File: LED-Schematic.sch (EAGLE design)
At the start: 12 parts, among them J1 POWER_JACKPTH, Q1 SUP75N06-08, Q2 SUP75N06-08, Q3 SUP75N06-08

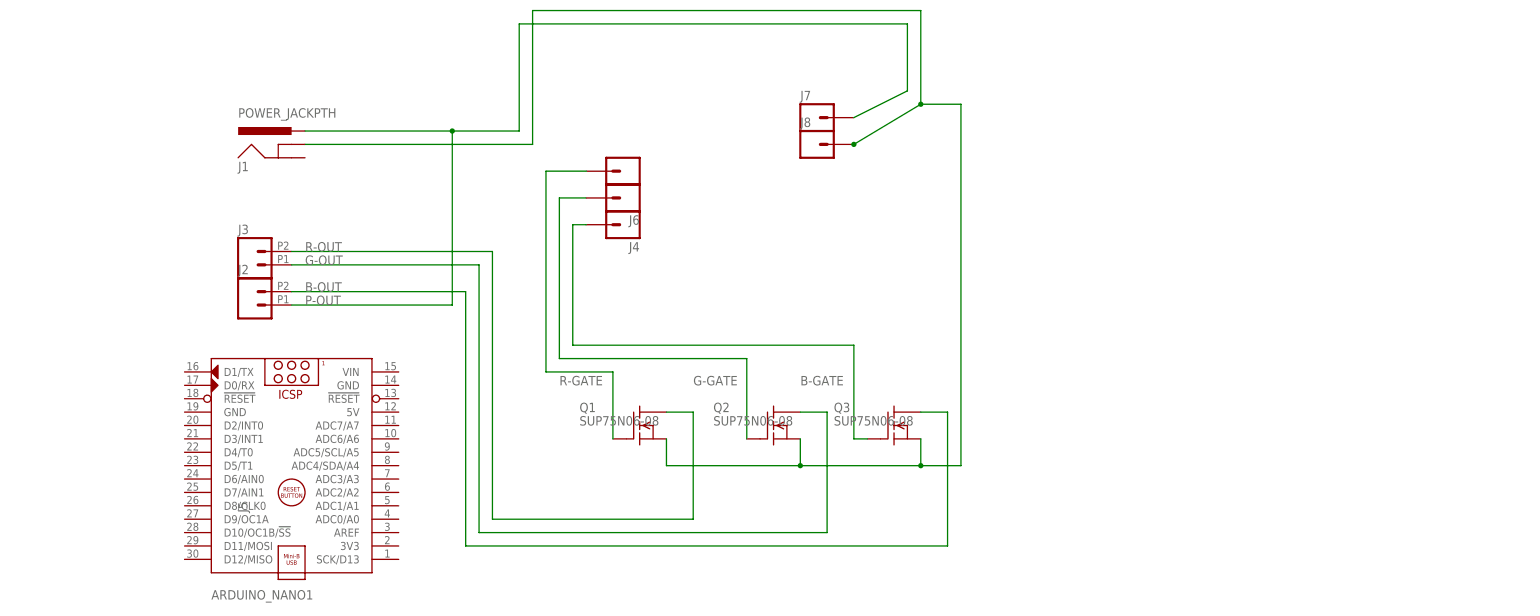
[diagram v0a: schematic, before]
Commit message: Added arduino to schematic, added PCB board, added gitignore
Signed-off-by: Maximilian Pult <it@optik-riede.de>
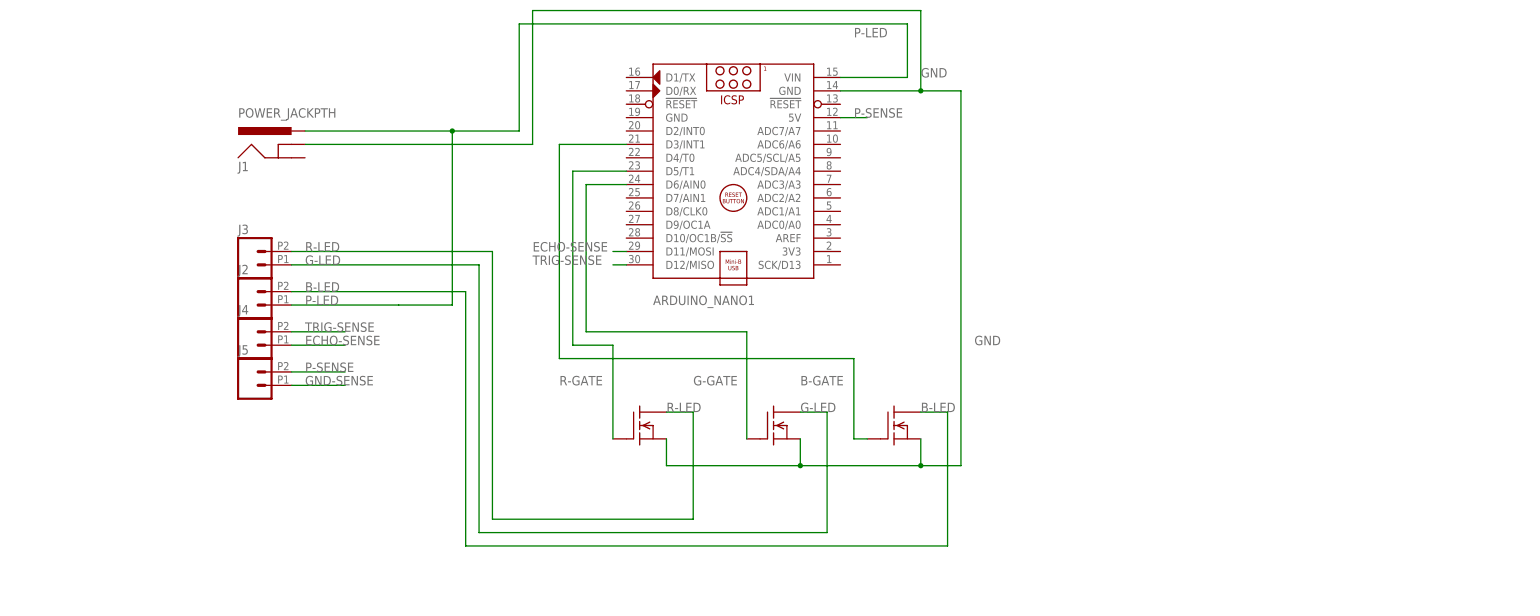
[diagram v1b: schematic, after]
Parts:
- removed J6, J7, J8: (no value), SparkFun-Connectors:M01SNAP-FEMALE
- J4, J5: device SparkFun-Connectors:M01SNAP-FEMALE -> SparkFun-Connectors:M022.54MM_SCREWTERM
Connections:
- net B-OUT renamed B-LED
- net G-OUT renamed G-LED
- net R-OUT renamed R-LED
- removed net N$3: J1.GNDBREAK, J8.1, Q1.S, Q2.S, Q3.S
- removed net P-OUT: J1.PWR, J2.1, J7.1
- new net ECHO-SENSE: ARDUINO_NANO1.D11/MOSI, J4.1
- new net GND: ARDUINO_NANO1.GND@2, J1.GNDBREAK, Q1.S, Q2.S, Q3.S
- new net GND-SENSE: J5.1
- new net P-LED: ARDUINO_NANO1.VIN, J1.PWR, J2.1
- new net P-SENSE: ARDUINO_NANO1.5V, J5.2
- new net TRIG-SENSE: ARDUINO_NANO1.D12/MISO, J4.2
- net B-GATE: now also ARDUINO_NANO1.D3/INT1; no longer J4.1
- net G-GATE: now also ARDUINO_NANO1.D6/AIN0; no longer J6.1
- net R-GATE: now also ARDUINO_NANO1.D5/T1; no longer J5.1
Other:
- moved on the sheet: ARDUINO_NANO1

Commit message: swapped mosfets to infineon IRLs
Signed-off-by: Maximilian Pult <it@optik-riede.de>
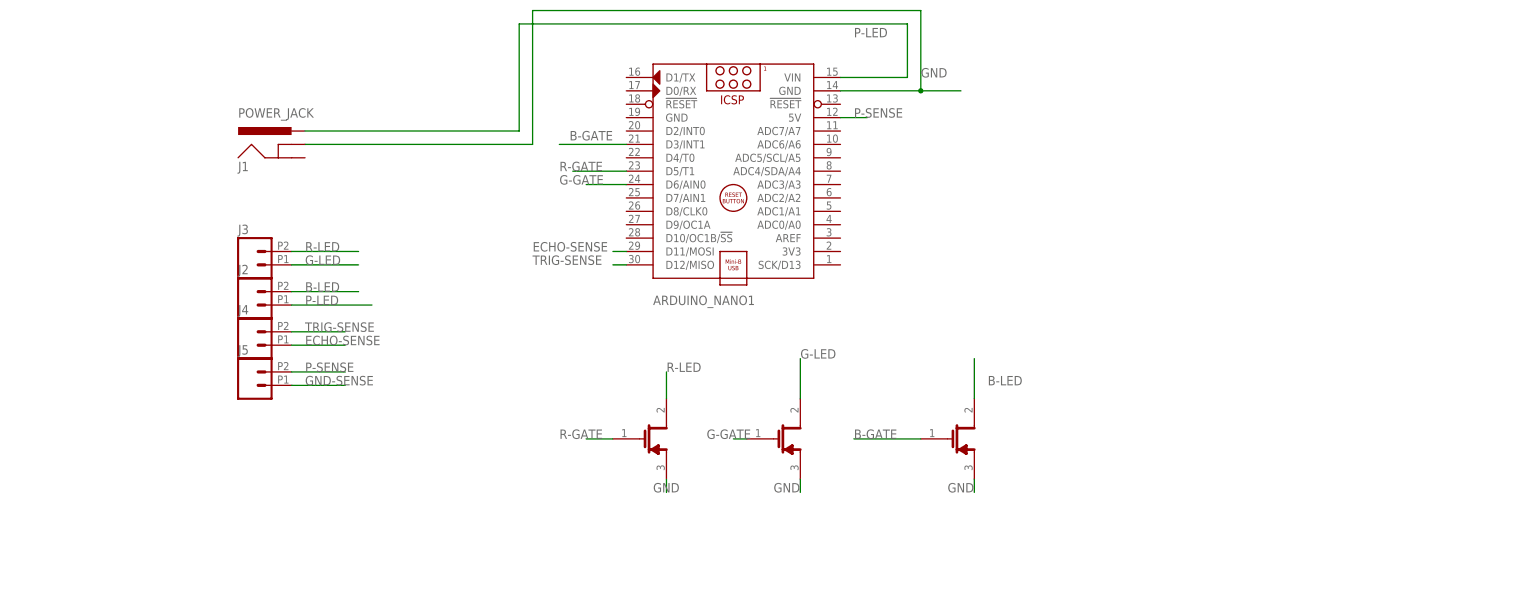
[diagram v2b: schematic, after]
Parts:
- J1: value POWER_JACKPTH -> POWER_JACK; device SparkFun-Connectors:POWER_JACKPTH -> SparkFun-Connectors:POWER_JACK
- Q1, Q2, Q3: value SUP75N06-08 -> INFINEON_IRLB8721PBFINFINEON_IRLB8721PBF_0_0; device transistor-fet:SUP75N06-08 -> Infineon - IRLB8721PbF:INFINEON_IRLB8721PBFINFINEON_IRLB8721PBF_0_0

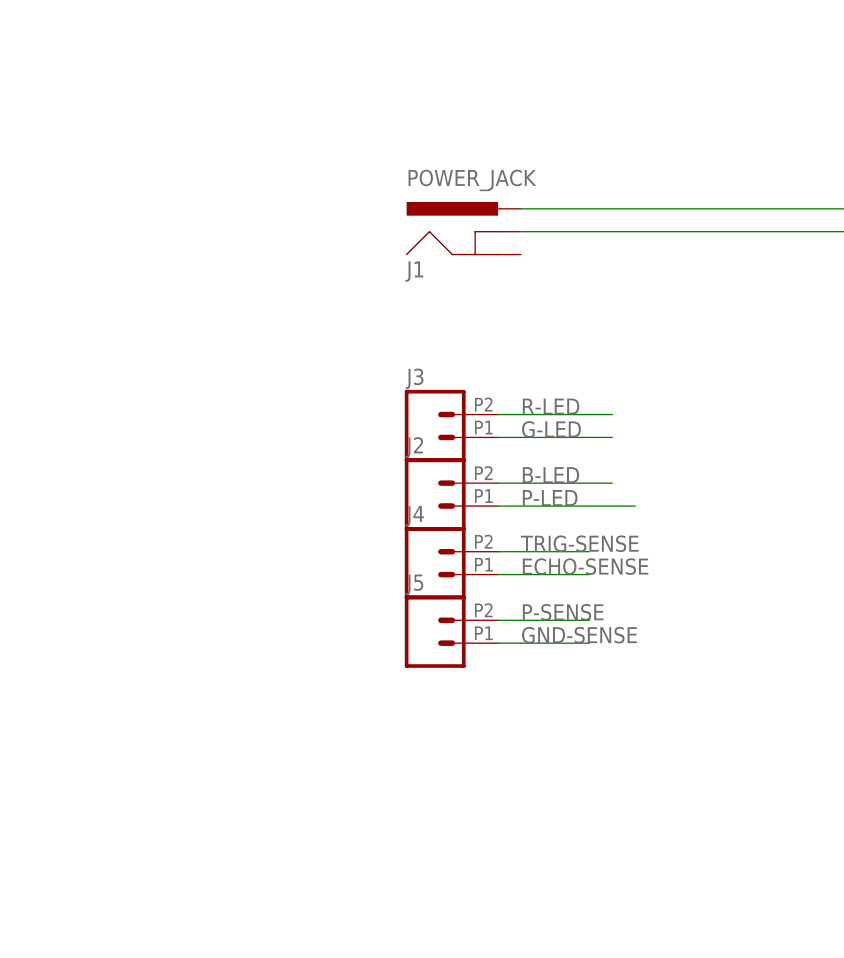
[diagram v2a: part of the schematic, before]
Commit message: Adding Datasheets, replace screw terms
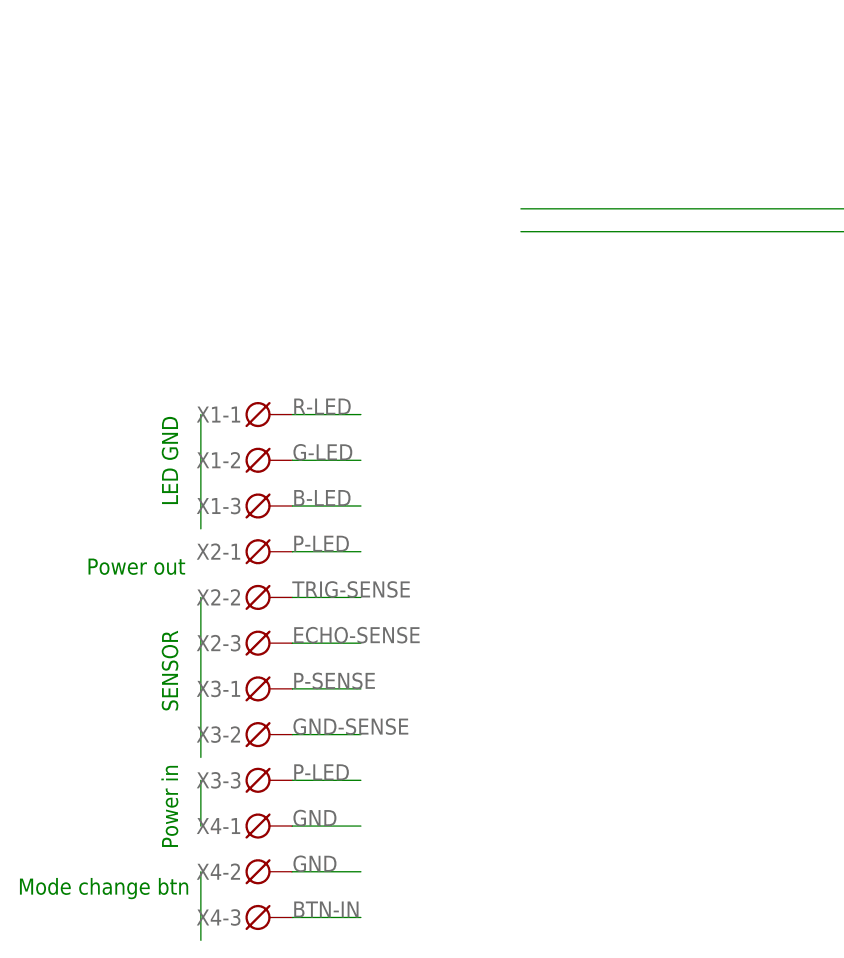
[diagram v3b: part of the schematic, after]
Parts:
- removed J1: POWER_JACK, SparkFun-Connectors:POWER_JACK
- removed J2, J3, J4, J5: (no value), SparkFun-Connectors:M022.54MM_SCREWTERM
- added X1, X2, X3, X4: DG3XX-03-3.5, degson:DG3XX-03-3.5
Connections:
- new net BTN-IN: X4-3.KL
- net B-LED: now also X1-3.KL; no longer J2.2
- net ECHO-SENSE: now also X2-3.KL; no longer J4.1
- net G-LED: now also X1-2.KL; no longer J3.1
- net GND: now also X4-1.KL, X4-2.KL; no longer J1.GNDBREAK
- net GND-SENSE: now also X3-2.KL; no longer J5.1
- net P-LED: now also X2-1.KL, X3-3.KL; no longer J1.PWR, J2.1
- net P-SENSE: now also X3-1.KL; no longer J5.2
- net R-LED: now also X1-1.KL; no longer J3.2
- net TRIG-SENSE: now also X2-2.KL; no longer J4.2
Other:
- note added: "LED GND"
- note added: "Mode change btn"
- note added: "Power in"
- note added: "Power out"
- note added: "SENSOR"

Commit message: Before reroute
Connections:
- removed net GND-SENSE: X3-2.KL
- net BTN-IN: now also ARDUINO_NANO1.D8/CLK0
- net GND: now also X3-2.KL
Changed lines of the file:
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@@
 <label x="-33.02" y="20.32" size="1.778" layer="95"/>
+</segment>
+<segment>
+<pinref part="X3" gate="-2" pin="KL"/>
+<wire x1="-33.02" y1="35.56" x2="-25.4" y2="35.56" width="0.1524" layer="91"/>
+<label x="-33.02" y="35.56" size="1.778" layer="95"/>
 </segment>
 </net>
@@
 </segment>
 </net>
-<net name="GND-SENSE" class="0">
-<segment>
-<pinref part="X3" gate="-2" pin="KL"/>
-<wire x1="-33.02" y1="35.56" x2="-25.4" y2="35.56" width="0.1524" layer="91"/>
-<label x="-33.02" y="35.56" size="1.778" layer="95"/>
-</segment>
-</net>
 <net name="BTN-IN" class="0">
 <segment>
@@
 <label x="-33.02" y="15.24" size="1.778" layer="95"/>
 </segment>
+<segment>
+<pinref part="ARDUINO_NANO1" gate="G$1" pin="D8/CLK0"/>
+<wire x1="53.34" y1="78.74" x2="45.72" y2="78.74" width="0.1524" layer="91"/>
+<label x="40.64" y="78.74" size="1.778" layer="95"/>
+</segment>
 </net>

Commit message: Last Revamp, i promise
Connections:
- net P-LED renamed 12V
- net P-SENSE renamed 5V
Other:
- note added: "LED OUT"
- note removed: "LED GND"
- note removed: "Power out"
- moved on the sheet: X1-1, X1-2, X1-3, X2-1, X2-2, X2-3, X3-1, X3-2, X3-3, X4-1, X4-2, X4-3

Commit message: Adding PCB Design export
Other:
- moved on the sheet: X1-1, X1-2, X1-3, X2-1, X2-2, X2-3, X3-1, X3-2, X3-3, X4-1, X4-2, X4-3

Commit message: Final Edits before production
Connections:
- new net 3.3V: ARDUINO_NANO1.3V3, X4-2.KL
- net GND: no longer X4-2.KL
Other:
- note added: "BTN-IN Is a jumper +3.3v: Strobe GND: Constant"
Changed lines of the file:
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@@
 <part name="X3" library="degson" deviceset="DG3XX-03" device="-3.5"/>
 <part name="X4" library="degson" deviceset="DG3XX-03" device="-3.5"/>
-<part name="GND1" library="SparkFun-Aesthetics" deviceset="GND" device=""/>
 <part name="GND2" library="SparkFun-Aesthetics" deviceset="GND" device=""/>
 <part name="GND3" library="SparkFun-Aesthetics" deviceset="GND" device=""/>
@@
 <part name="SUPPLY5" library="SparkFun-Aesthetics" deviceset="12V" device=""/>
 <part name="FRAME1" library="frames" library_urn="urn:adsk.eagle:library:229" deviceset="DINA4_L" device=""/>
+<part name="SUPPLY6" library="SparkFun-Aesthetics" deviceset="3.3V" device=""/>
+<part name="SUPPLY7" library="SparkFun-Aesthetics" deviceset="3.3V" device=""/>
 </parts>
 <sheets>
@@
 <text x="-15.24" y="55.88" size="1.778" layer="91" rot="R90">SENSOR</text>
 <text x="-15.24" y="78.74" size="1.778" layer="91" rot="R90">LED OUT</text>
+<text x="182.88" y="22.86" size="2.54" layer="97">BTN-IN Is a jumper
++3.3v: Strobe
+GND: Constant</text>
 </plain>
 <instances>
@@
 <attribute name="NAME" x="-8.128" y="29.591" size="1.778" layer="95" rot="MR0"/>
 </instance>
-<instance part="GND1" gate="1" x="7.62" y="35.56" smashed="yes" rot="R90">
-<attribute name="VALUE" x="10.16" y="35.56" size="1.778" layer="96"/>
-</instance>
 <instance part="GND2" gate="1" x="7.62" y="40.64" smashed="yes" rot="R90">
 <attribute name="VALUE" x="10.16" y="40.64" size="1.778" layer="96"/>
@@
 <attribute name="DRAWING_NAME" x="129.54" y="3.81" size="2.54" layer="94"/>
 </instance>
+<instance part="SUPPLY6" gate="G$1" x="106.68" y="71.12" smashed="yes" rot="R270">
+<attribute name="VALUE" x="110.236" y="72.136" size="1.778" layer="96" rot="R270"/>
+</instance>
+<instance part="SUPPLY7" gate="G$1" x="5.08" y="35.56" smashed="yes" rot="R270">
+<attribute name="VALUE" x="8.636" y="36.576" size="1.778" layer="96" rot="R270"/>
+</instance>
 </instances>
 <busses>
@@
 </segment>
 <segment>
-<pinref part="X4" gate="-2" pin="KL"/>
-<wire x1="-2.54" y1="35.56" x2="5.08" y2="35.56" width="0.1524" layer="91"/>
-<pinref part="GND1" gate="1" pin="GND"/>
-</segment>
-<segment>
 <pinref part="X3" gate="-2" pin="KL"/>
 <wire x1="-2.54" y1="53.34" x2="5.08" y2="53.34" width="0.1524" layer="91"/>
@@
 </segment>
 </net>
+<net name="3.3V" class="0">
+<segment>
+<pinref part="X4" gate="-2" pin="KL"/>
+<wire x1="-2.54" y1="35.56" x2="5.08" y2="35.56" width="0.1524" layer="91"/>
+<pinref part="SUPPLY7" gate="G$1" pin="3.3V"/>
+</segment>
+<segment>
+<pinref part="ARDUINO_NANO1" gate="G$1" pin="3V3"/>
+<pinref part="SUPPLY6" gate="G$1" pin="3.3V"/>
+<wire x1="93.98" y1="71.12" x2="106.68" y2="71.12" width="0.1524" layer="91"/>
+</segment>
+</net>
